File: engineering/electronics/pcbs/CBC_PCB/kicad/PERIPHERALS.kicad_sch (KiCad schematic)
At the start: 7 parts, among them J2 AT13-12PB-BM03

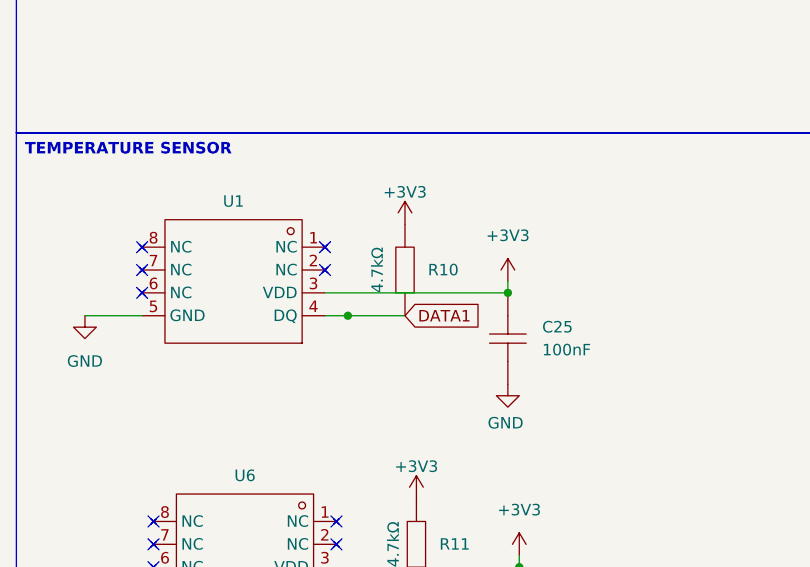
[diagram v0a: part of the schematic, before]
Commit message: fix: add CBC peripheral sensor power flag
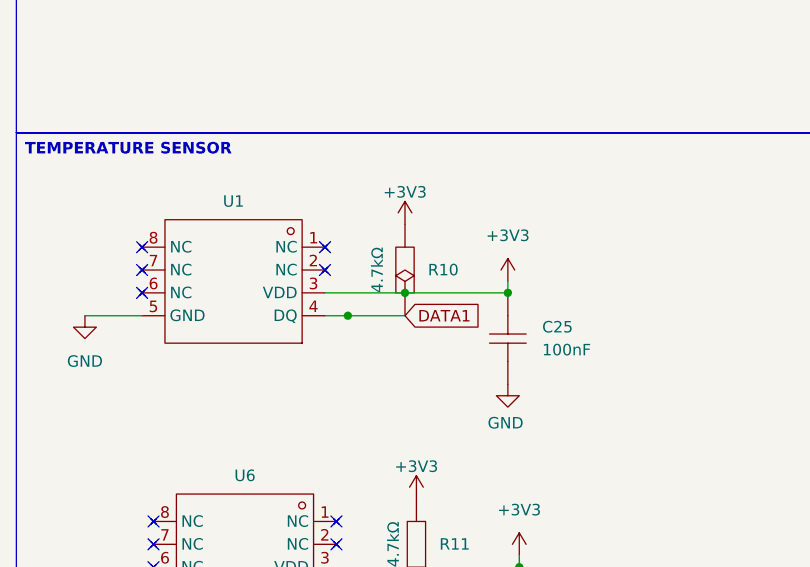
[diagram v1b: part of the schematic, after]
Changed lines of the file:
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@@
+	)
+	(junction
+		(at 55.88 135.89)
+		(diameter 0)
+		(color 0 0 0 0)
 	)
 	(junction
@@
 					(unit 1)
 				)
+			)
+		)
+	)
+	(symbol
+		(lib_id "power:PWR_FLAG")
+		(at 55.88 135.89 0)
+		(unit 1)
+		(body_style 1)
+		(exclude_from_sim no)
+		(in_bom yes)
+		(on_board yes)
+		(in_pos_files yes)
+		(dnp no)
+		(fields_autoplaced yes)
+		(property "Reference" "#FLG069"
+			(at 55.88 133.985 0)
+			(hide yes)
+			(show_name no)
+			(do_not_autoplace no)
+			(effects
+				(font
+					(size 1.27 1.27)
+				)
+			)
+		)
+		(property "Value" "PWR_FLAG"
+			(at 55.88 130.81 0)
+			(hide yes)
+			(show_name no)
+			(do_not_autoplace no)
+			(effects
+				(font
+					(size 1.27 1.27)
+				)
+			)
+		)
+		(property "Footprint" ""
+			(at 55.88 135.89 0)
+			(hide yes)
+			(show_name no)
+			(do_not_autoplace no)
+			(effects
+				(font
+					(size 1.27 1.27)
+				)
+			)
+		)
+		(property "Datasheet" ""
+			(at 55.88 135.89 0)
+			(hide yes)
+			(show_name no)
+			(do_not_autoplace no)
+			(effects
+				(font
+					(size 1.27 1.27)
+				)
+			)
+		)
+		(property "Description" "Special symbol for telling ERC where power comes from"
+			(at 55.88 135.89 0)
+			(hide yes)
+			(show_name no)
+			(do_not_autoplace no)
+			(effects
+				(font
+					(size 1.27 1.27)
+				)
+			)
+		)
+		(pin "1"
+		)
+		(instances
+			(project "CBC_PCB"
+				(path "/d195d1ee-585b-4211-912f-f5dd5687bc63/b4c95d27-7981-477f-a8ef-d2ce83f3675e"
+					(reference "#FLG069")
+					(unit 1)
+				)

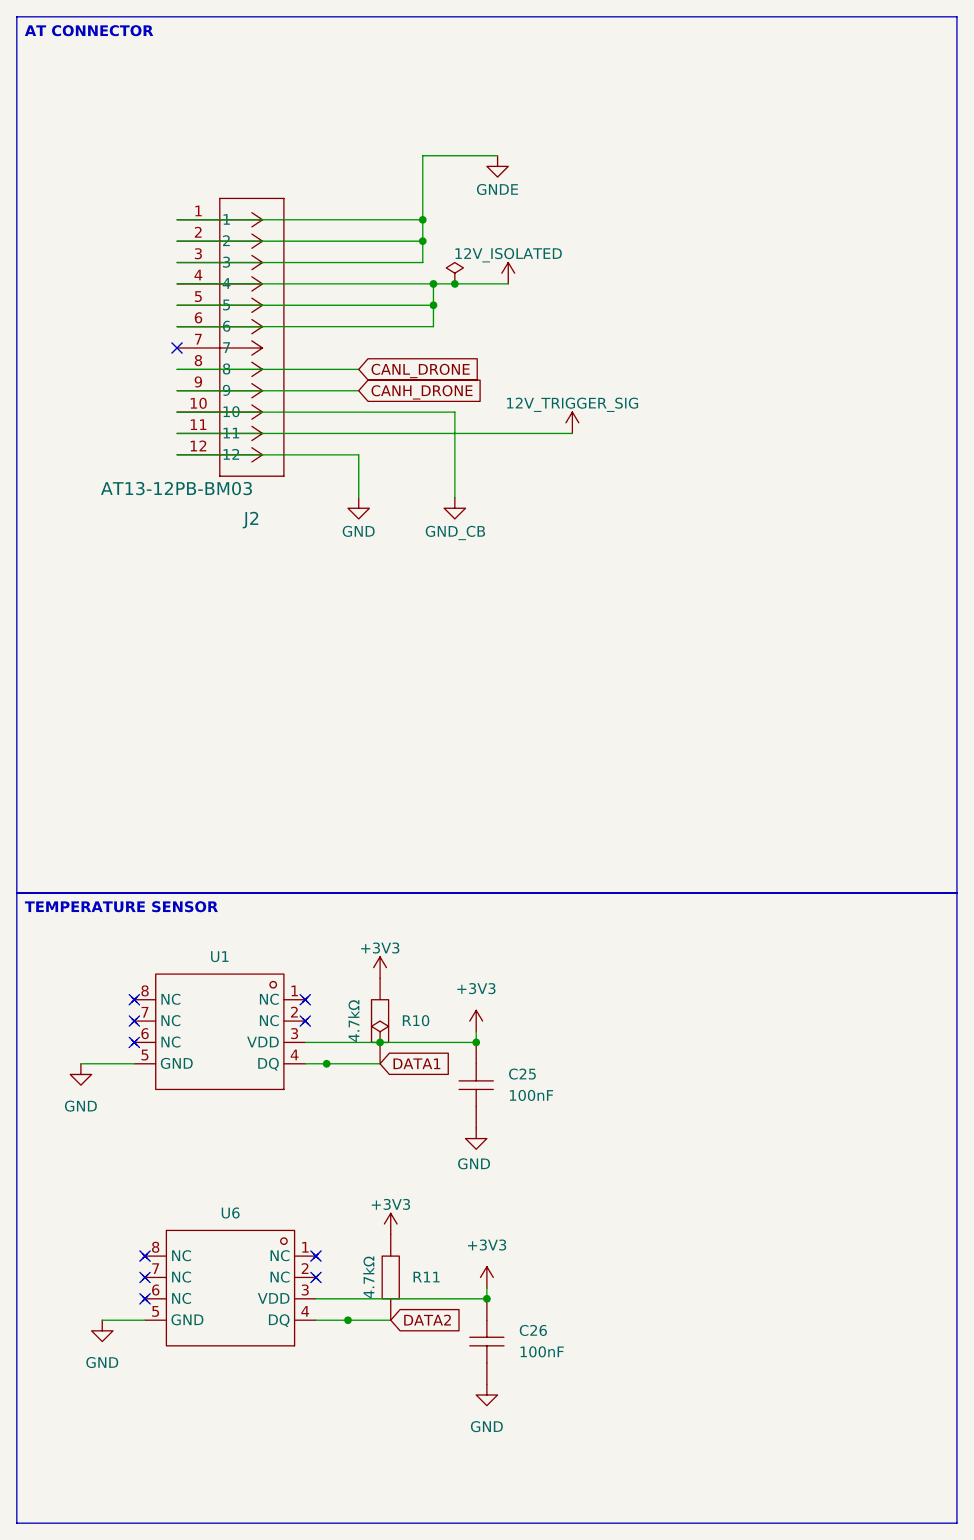
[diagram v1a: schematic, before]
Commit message: docs: capture CBC schematic review follow-ups
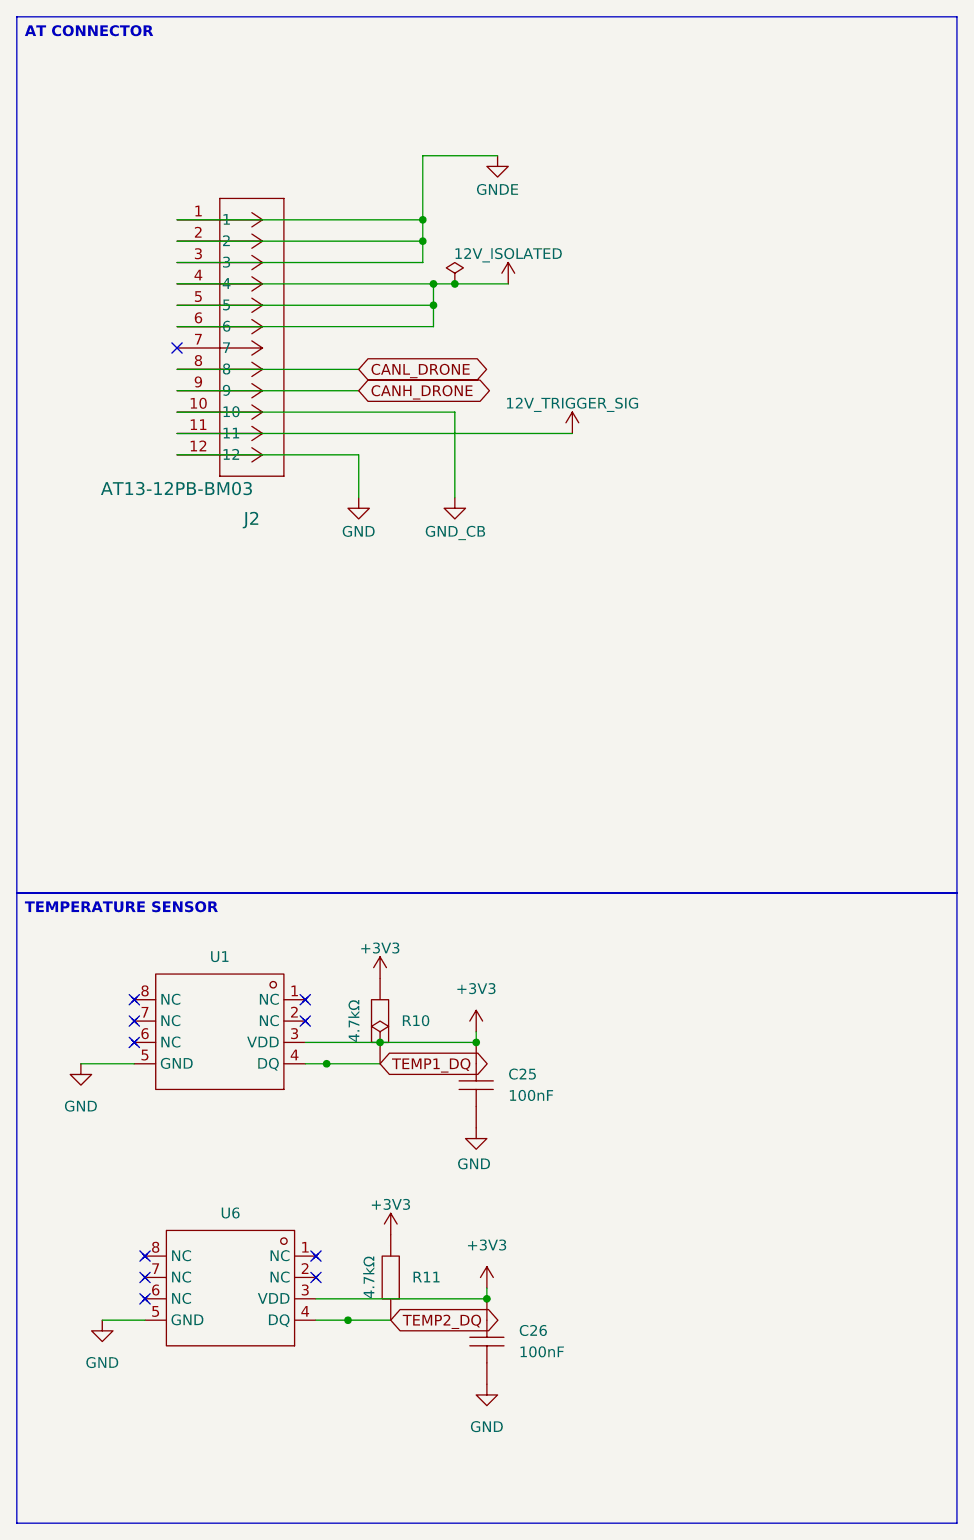
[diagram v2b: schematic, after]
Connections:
- net DATA1 renamed TEMP1_DQ
- net DATA2 renamed TEMP2_DQ
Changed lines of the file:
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@@
 	)
 	(global_label "CANL_DRONE"
-		(shape input)
+		(shape bidirectional)
 		(at 53.34 55.88 0)
 		(fields_autoplaced yes)
@@
 		)
 	)
-	(global_label "DATA1"
-		(shape input)
+	(global_label "TEMP1_DQ"
+		(shape bidirectional)
 		(at 55.88 138.43 0)
 		(fields_autoplaced yes)
@@
 		)
 	)
-	(global_label "DATA2"
-		(shape input)
+	(global_label "TEMP2_DQ"
+		(shape bidirectional)
 		(at 57.15 168.91 0)
 		(fields_autoplaced yes)
@@
 	)
 	(global_label "CANH_DRONE"
-		(shape input)
+		(shape bidirectional)
 		(at 53.34 58.42 0)
 		(fields_autoplaced yes)
